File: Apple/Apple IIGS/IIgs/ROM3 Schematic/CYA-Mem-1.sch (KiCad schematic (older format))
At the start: 28 parts, among them J20 IIgs_Memory_Connector, U6 65SC816

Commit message: More label style changes
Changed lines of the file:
@@
 Text Label 2950 3550 2    50   ~ 0
 PH2D.H
-Text GLabel 3750 3550 2    50   Input ~ 0
-PH2.H
-Text GLabel 2850 4100 2    50   Input ~ 0
-NMI.L
-Text GLabel 2850 4250 2    50   Input ~ 0
-RDY.H
 $Comp
 L Device:R_Small R133
@@
 Wire Wire Line
 	4450 4450 4750 4450
-Text GLabel 2850 4400 2    50   Input ~ 0
-RESET.L
 Wire Wire Line
 	2850 4400 2600 4400
@@
 Text Label 4400 5050 0    50   ~ 0
 RESET.L
-Text GLabel 4050 4850 0    50   Input ~ 0
-STRETCH.L
 Wire Wire Line
 	4050 4850 4150 4850
@@
 Text Label 1300 4150 0    50   ~ 0
 VP
-Text GLabel 2850 4550 2    50   Input ~ 0
-IRQ.L
 Wire Wire Line
 	2600 4550 2850 4550
@@
 Wire Wire Line
 	1100 3350 1550 3350
-Text GLabel 4450 4000 0    50   Input ~ 0
-PH2.H
-Text GLabel 4450 4300 0    50   Input ~ 0
-RDY.H
-Text GLabel 3850 4650 0    50   Input ~ 0
-NMI.L
 $Comp
 L Device:R_Small R6
@@
 Wire Wire Line
 	1100 2950 1100 3050
-Text GLabel 6700 1200 2    50   Input ~ 0
-M2BA0
 Wire Wire Line
 	6150 1200 6350 1200
@@
 	0    1    1    0
 $EndComp
-Text GLabel 7500 2550 2    50   Input ~ 0
-CASD
 $Comp
 L Connector:TestPoint TP95
@@
 	1    0    0    -1
 $EndComp
-Text GLabel 7500 2400 2    50   Input ~ 0
-RASD
 Connection ~ 6700 2400
 Wire Wire Line
@@
 Wire Wire Line
 	6150 3800 6600 3800
-Text GLabel 6600 3800 2    50   Input ~ 0
-14MD.H
 Wire Wire Line
 	6150 3950 6600 3950
@@
 Wire Wire Line
 	6150 4250 6600 4250
-Text GLabel 6600 3950 2    50   Input ~ 0
-ROMSEL1.L
-Text GLabel 6600 4100 2    50   Input ~ 0
-ROMOE-A16D
-Text GLabel 6600 4250 2    50   Input ~ 0
-ROMSEL0.L
 $Comp
 L Device:R_Small R31
@@
 	0    1    1    0
 $EndComp
-Text GLabel 7000 4450 2    50   Input ~ 0
-ROMSEL0.L
 Wire Wire Line
 	7000 4450 6900 4450
@@
 Wire Wire Line
 	6150 4650 6600 4650
-Text GLabel 6600 4650 2    50   Input ~ 0
-A2R-W.H
-Text GLabel 6600 4850 2    50   Input ~ 0
-DMA.L
-Text GLabel 6600 5050 2    50   Input ~ 0
-DBDIR.L
 Wire Wire Line
 	6150 4850 6300 4850
@@
 Wire Wire Line
 	6600 5050 6150 5050
-Text GLabel 6600 5250 2    50   Input ~ 0
-DBENB.L
 Wire Wire Line
 	6600 5250 6150 5250
-Text GLabel 6600 5450 2    50   Input ~ 0
-ABENB.L
 Wire Wire Line
 	6600 5450 6150 5450
-Text GLabel 6600 5650 2    50   Input ~ 0
-ABDIR.L
 Wire Wire Line
 	6600 5650 6150 5650
@@
 Wire Wire Line
 	8550 6050 8850 6050
-Text GLabel 8850 6050 2    50   Input ~ 0
-fastRR-W.H
 Wire Wire Line
 	8050 4800 8050 6050
@@
 Text Notes 5650 850  0    50   ~ 0
 CYA aka FPI
+Text HLabel 2850 4550 2    50   Input ~ 0
+IRQ.L
+Text HLabel 2850 4400 2    50   Input ~ 0
+RESET.L
+Text HLabel 2850 4250 2    50   Input ~ 0
+RDY.H
+Text HLabel 2850 4100 2    50   Input ~ 0
+NMI.L
+Text HLabel 3750 3550 2    50   Input ~ 0
+PH2.H
+Text HLabel 4450 4000 0    50   Input ~ 0
+PH2.H
+Text HLabel 4450 4300 0    50   Input ~ 0
+RDY.H
+Text HLabel 3850 4650 0    50   Input ~ 0
+NMI.L
+Text HLabel 4050 4850 0    50   Input ~ 0
+STRETCH.L
+Text HLabel 6600 5650 2    50   Input ~ 0
+ABDIR.L
+Text HLabel 6600 5450 2    50   Input ~ 0
+ABENB.L
+Text HLabel 6600 5250 2    50   Input ~ 0
+DBENB.L
+Text HLabel 6600 5050 2    50   Input ~ 0
+DBDIR.L
+Text HLabel 6600 4850 2    50   Input ~ 0
+DMA.L
+Text HLabel 6600 4650 2    50   Input ~ 0
+A2R-W.H
+Text HLabel 7000 4450 2    50   Input ~ 0
+ROMSEL0.L
+Text HLabel 6600 4250 2    50   Input ~ 0
+ROMSEL0.L
+Text HLabel 6600 4100 2    50   Input ~ 0
+ROMOE-A16D
+Text HLabel 6600 3950 2    50   Input ~ 0
+ROMSEL1.L
+Text HLabel 6600 3800 2    50   Input ~ 0
+14MD.H
+Text HLabel 7500 2550 2    50   Input ~ 0
+CASD
+Text HLabel 7500 2400 2    50   Input ~ 0
+RASD
+Text HLabel 6700 1200 2    50   Input ~ 0
+M2BA0
+Text HLabel 8850 6050 2    50   Input ~ 0
+fastRR-W.H
 $EndSCHEMATC

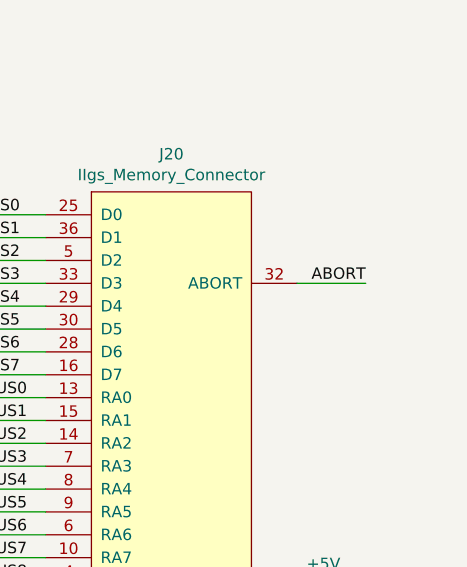
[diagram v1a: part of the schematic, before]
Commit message: More hierarchical symbols added. changed symbol colors on CPU page
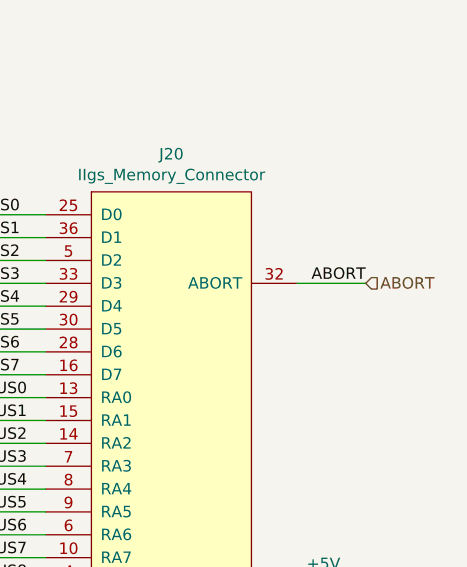
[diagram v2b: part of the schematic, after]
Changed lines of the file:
@@
 Text HLabel 8850 6050 2    50   Input ~ 0
 fastRR-W.H
+Text HLabel 10350 2700 2    50   Input ~ 0
+ABORT
 $EndSCHEMATC
